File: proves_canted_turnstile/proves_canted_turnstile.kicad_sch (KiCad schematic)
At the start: 11 parts, among them J1 Conn_Coaxial, U1 QBA-07+, U2 QBA-07+, U3 QBA-07+

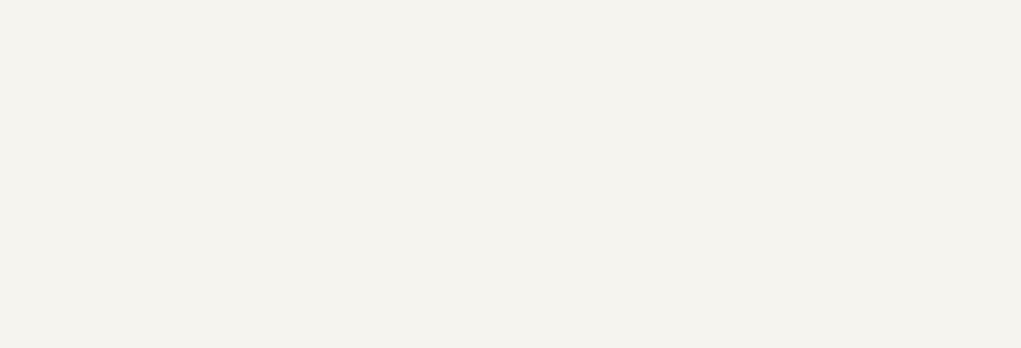
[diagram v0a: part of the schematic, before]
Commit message: assigned footprints to symbols and imported fiducials
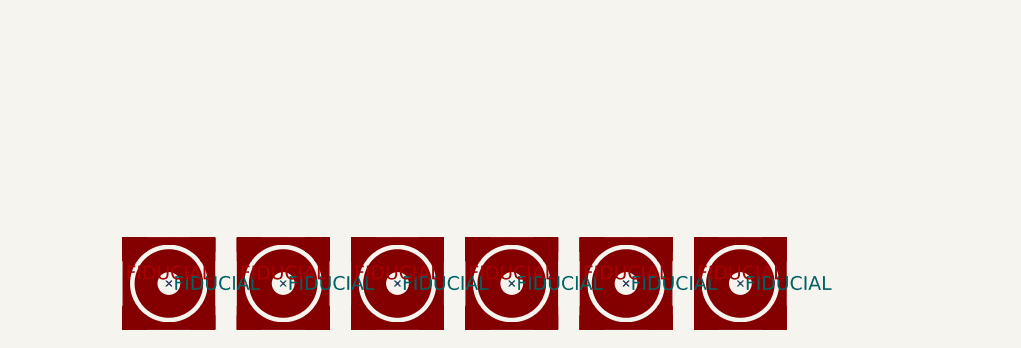
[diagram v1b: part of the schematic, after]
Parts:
- added FIDUCIAL1, FIDUCIAL2, FIDUCIAL3, FIDUCIAL4, FIDUCIAL6, FIDUCIAL7: FIDUCIAL-1.0X2.0, plusz-end-card-with-turnstile-mezzanine-eagle-import:FIDUCIAL-1.0X2.0, symbol plusz-end-card-with-turnstile-mezzanine-eagle-import:FIDUCIAL-1.0X2.0
- R1, R2, R3: footprint plusz-end-card-with-turnstile-mezzanine:.0603-C-NOSILK -> plusz-end-card-with-turnstile-mezzanine-eagle-import:.0603-C-NOSILK
- U1, U2, U3: footprint plusz-end-card-with-turnstile-mezzanine:QBA-07+ -> plusz-end-card-with-turnstile-mezzanine-eagle-import:QBA-07+

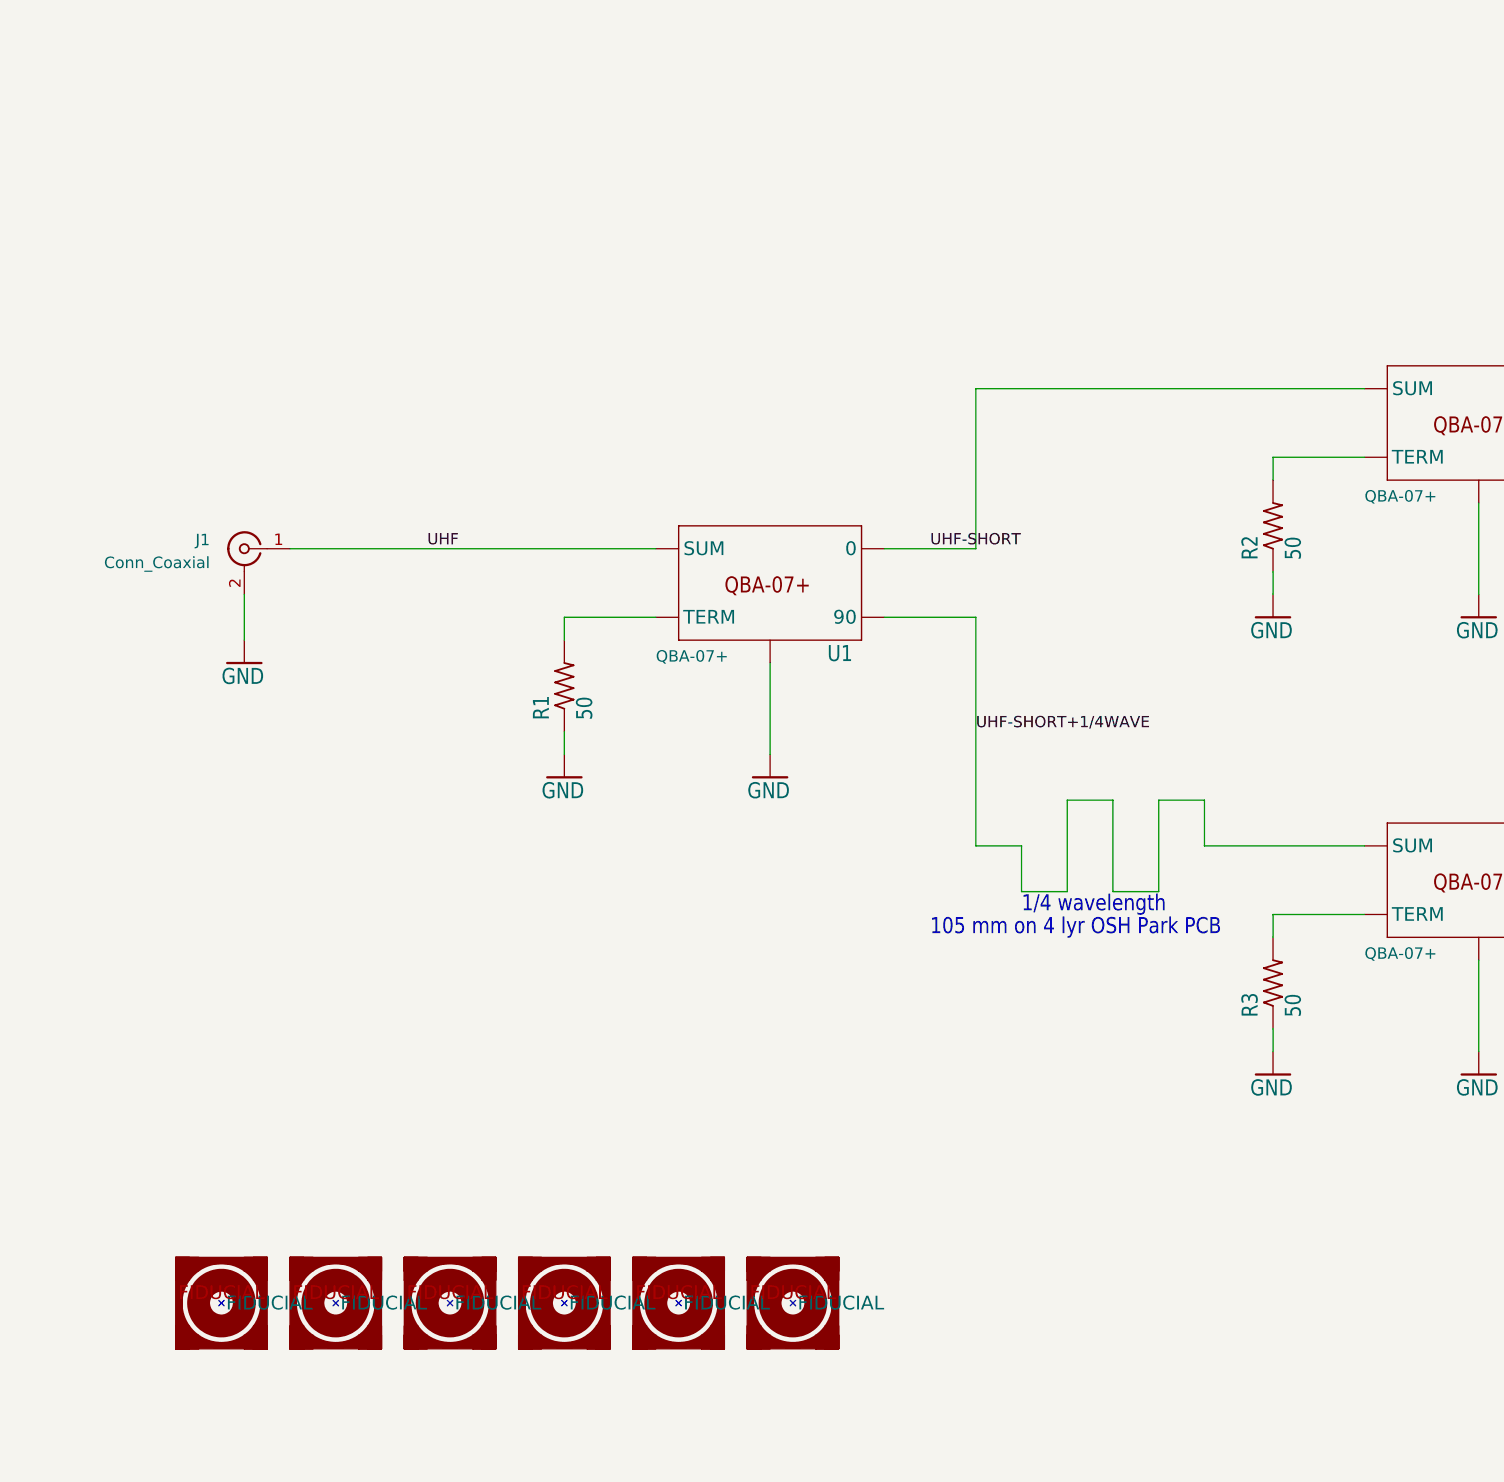
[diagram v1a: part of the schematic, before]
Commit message: implemented burnwire in schematic
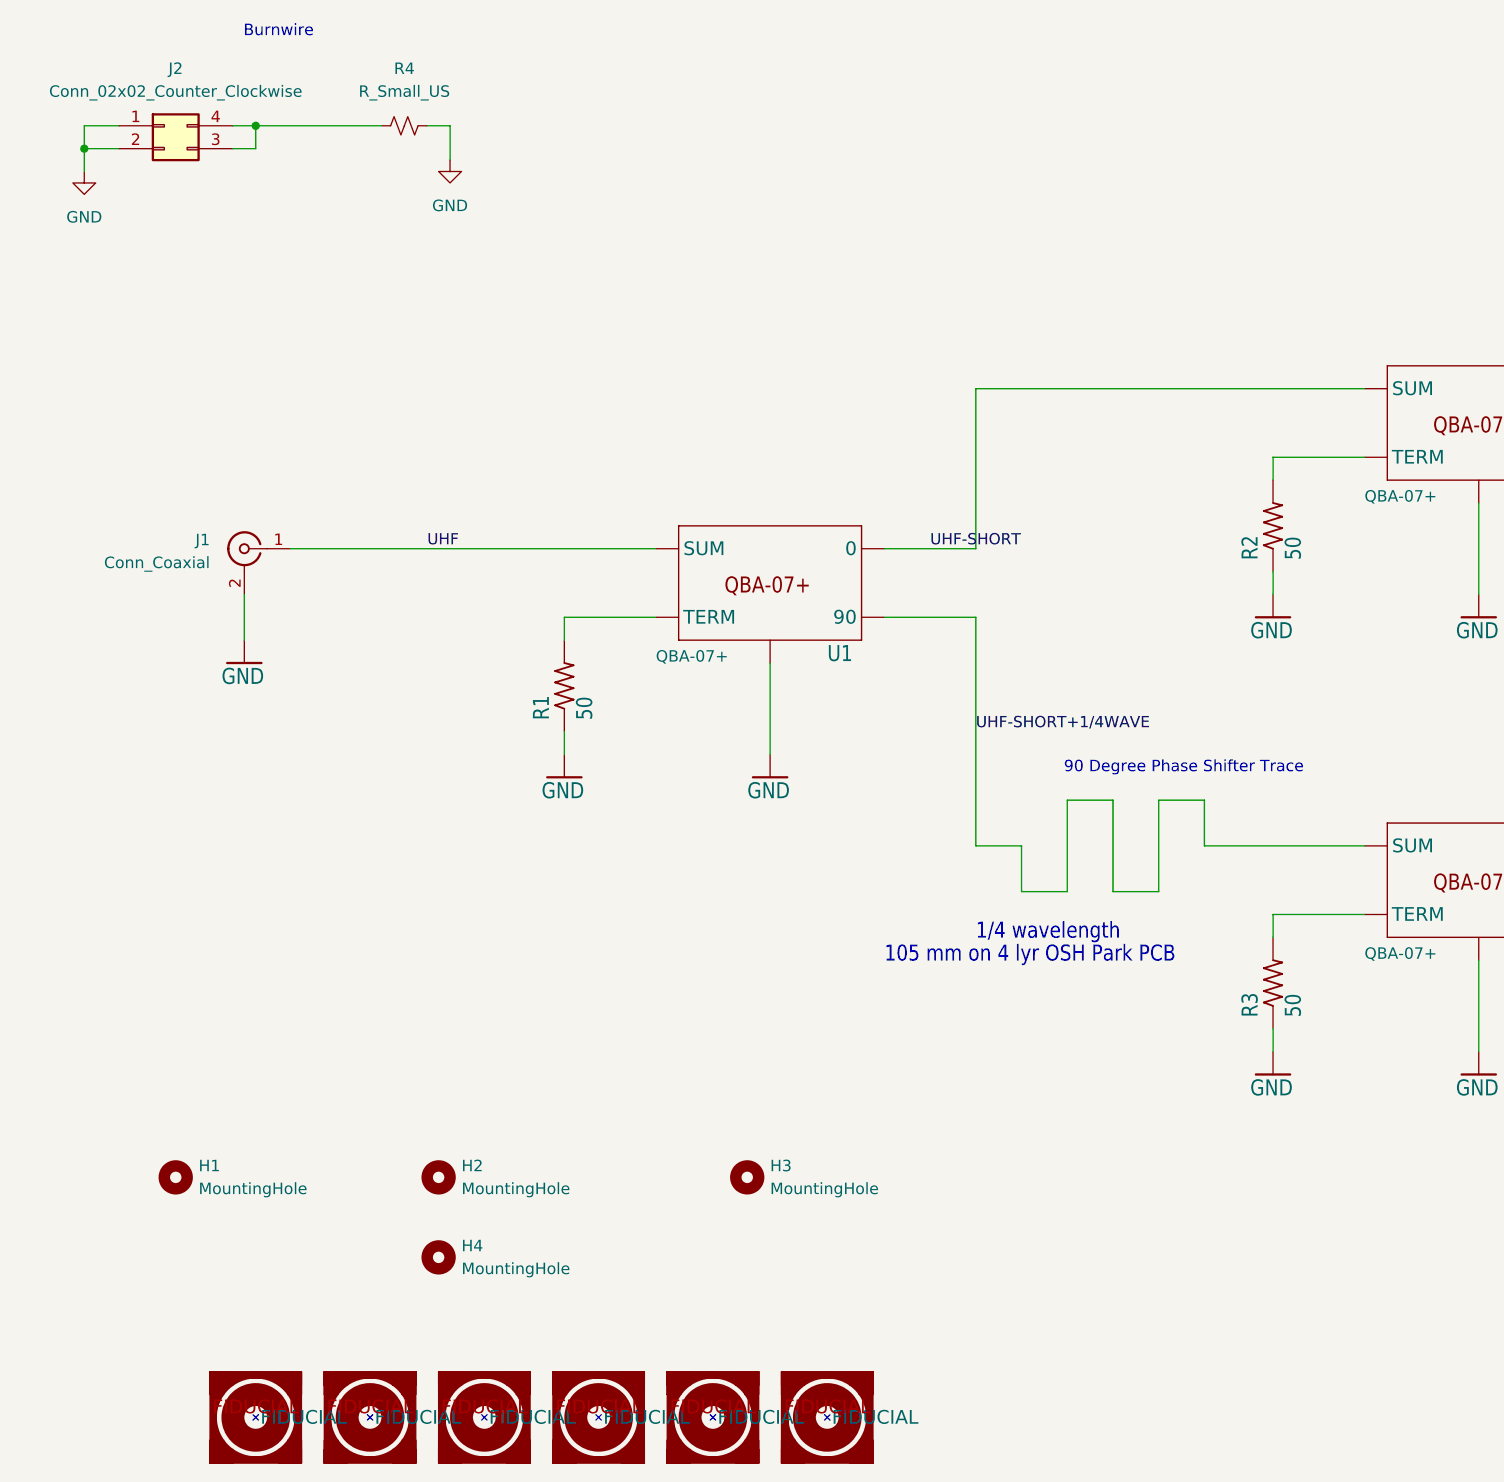
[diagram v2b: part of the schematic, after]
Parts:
- added H1, H2, H3, H4: MountingHole, MountingHole:MountingHole_2.7mm_M2.5_Pad, symbol Mechanical:MountingHole
- added J2: Conn_02x02_Counter_Clockwise, symbol Connector_Generic:Conn_02x02_Counter_Clockwise
- added R4: R_Small_US, symbol Device:R_Small_US
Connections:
- net GND: now also J2.1 (Pin_1), J2.2 (Pin_2), R4.2
- new net: J2.3 (Pin_3), J2.4 (Pin_4), R4.1
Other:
- note added: "90 Degree Phase Shifter Trace"
- note added: "Burnwire"

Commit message: updates
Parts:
- J2: footprint (none) -> Connector_Hirose:Hirose_DF11-4DP-2DSA_2x02_P2.00mm_Vertical
- R4: footprint (none) -> Resistor_THT:R_Axial_DIN0411_L9.9mm_D3.6mm_P25.40mm_Horizontal
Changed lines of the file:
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@@
 			)
 		)
-		(property "Footprint" ""
+		(property "Footprint" "Resistor_THT:R_Axial_DIN0411_L9.9mm_D3.6mm_P25.40mm_Horizontal"
 			(at 64.77 29.21 0)
 			(effects
@@
 			)
 		)
-		(property "Footprint" ""
+		(property "Footprint" "Connector_Hirose:Hirose_DF11-4DP-2DSA_2x02_P2.00mm_Vertical"
 			(at 38.1 29.21 0)
 			(effects

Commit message: changed trace widths
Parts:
- AE1, AE2, AE3, AE4: footprint Turnstile_Library:Singular_Tape_Measure_Antenna -> plusz-end-card-with-turnstile-mezzanine-eagle-import:Singular Tape Measure
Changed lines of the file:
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@@
 			)
 		)
-		(property "Footprint" "Turnstile_Library:Singular_Tape_Measure_Antenna"
+		(property "Footprint" "plusz-end-card-with-turnstile-mezzanine-eagle-import:Singular Tape Measure"
 			(at 237.49 66.04 0)
 			(effects
@@
 			)
 		)
-		(property "Footprint" "Turnstile_Library:Singular_Tape_Measure_Antenna"
+		(property "Footprint" "plusz-end-card-with-turnstile-mezzanine-eagle-import:Singular Tape Measure"
 			(at 237.49 111.76 0)
 			(effects
@@
 			)
 		)
-		(property "Footprint" "Turnstile_Library:Singular_Tape_Measure_Antenna"
+		(property "Footprint" "plusz-end-card-with-turnstile-mezzanine-eagle-import:Singular Tape Measure"
 			(at 237.49 43.18 0)
 			(effects
@@
 			)
 		)
-		(property "Footprint" "Turnstile_Library:Singular_Tape_Measure_Antenna"
+		(property "Footprint" "plusz-end-card-with-turnstile-mezzanine-eagle-import:Singular Tape Measure"
 			(at 237.49 88.9 0)
 			(effects

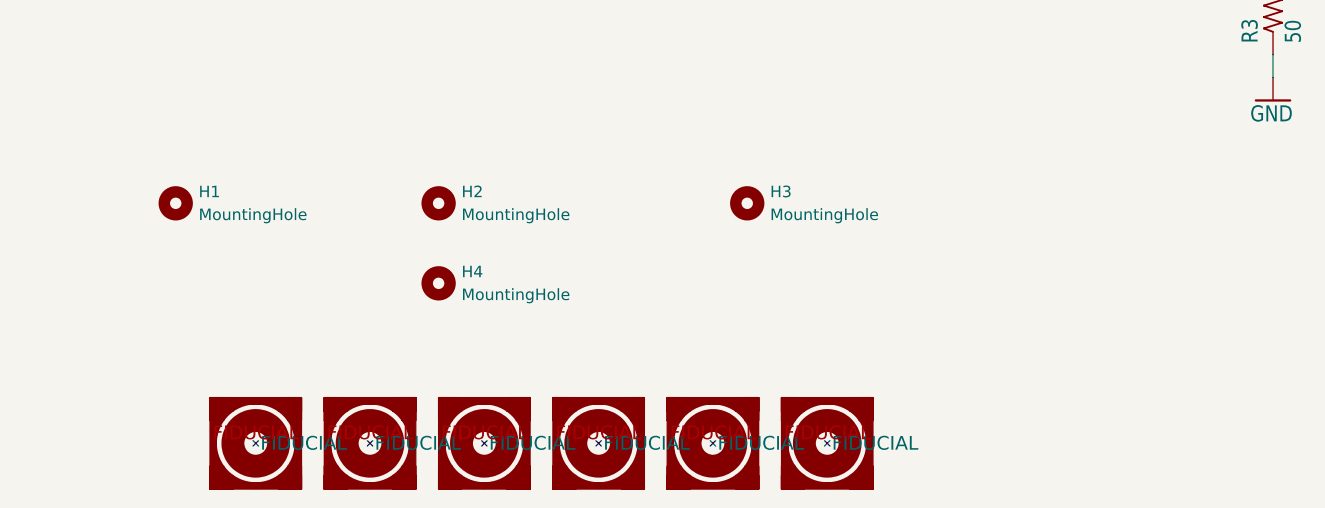
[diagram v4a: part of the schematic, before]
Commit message: placed mounting holes
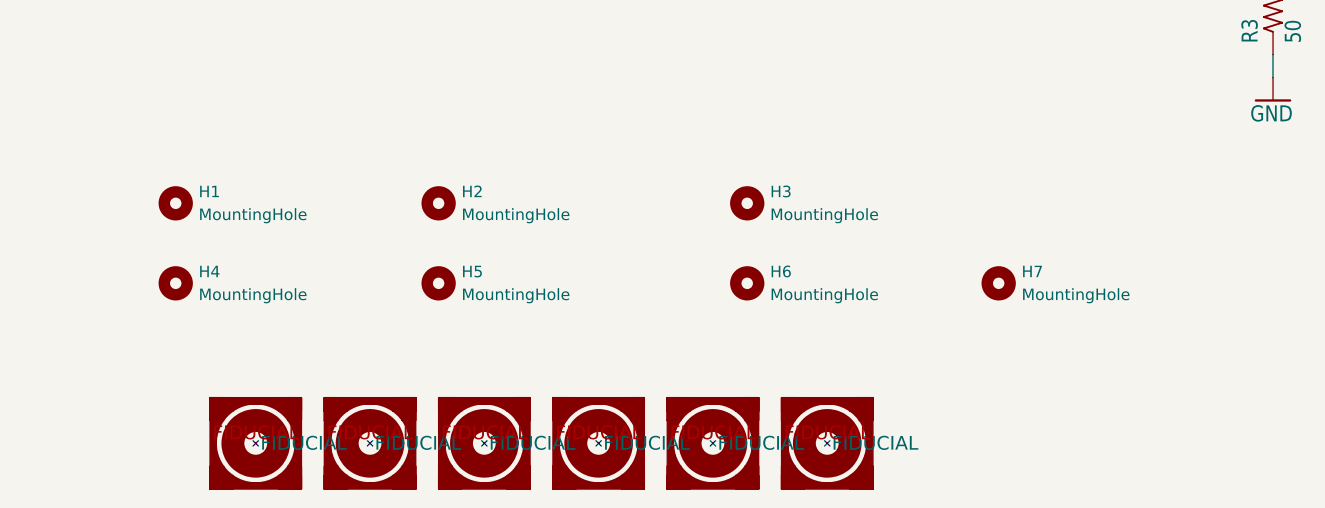
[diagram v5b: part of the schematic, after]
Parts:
- added H5, H6, H7: MountingHole, MountingHole:MountingHole_2.7mm_M2.5_Pad, symbol Mechanical:MountingHole
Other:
- moved on the sheet: H4
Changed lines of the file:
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@@
+	)
+	(symbol
+		(lib_id "Mechanical:MountingHole")
+		(at 102.87 154.94 0)
+		(unit 1)
+		(exclude_from_sim yes)
+		(in_bom no)
+		(on_board yes)
+		(dnp no)
+		(fields_autoplaced yes)
+		(property "Reference" "H6"
+			(at 105.41 153.6699 0)
+			(effects
+				(font
+					(size 1.27 1.27)
+				)
+				(justify left)
+			)
+		)
+		(property "Value" "MountingHole"
+			(at 105.41 156.2099 0)
+			(effects
+				(font
+					(size 1.27 1.27)
+				)
+				(justify left)
+			)
+		)
+		(property "Footprint" "MountingHole:MountingHole_2.7mm_M2.5_Pad"
+			(at 102.87 154.94 0)
+			(effects
+				(font
+					(size 1.27 1.27)
+				)
+				(hide yes)
+			)
+		)
+		(property "Datasheet" "~"
+			(at 102.87 154.94 0)
+			(effects
+				(font
+					(size 1.27 1.27)
+				)
+				(hide yes)
+			)
+		)
+		(property "Description" "Mounting Hole without connection"
+			(at 102.87 154.94 0)
+			(effects
+				(font
+					(size 1.27 1.27)
+				)
+				(hide yes)
+			)
+		)
+		(instances
+			(project "proves_canted_turnstile"
+				(path "/b0a1b345-df47-405c-b751-07790b55dab3"
+					(reference "H6")
+					(unit 1)
+				)
+			)
+		)
 	)
 	(symbol
@@
 	(symbol
 		(lib_id "Mechanical:MountingHole")
-		(at 68.58 154.94 0)
+		(at 39.37 154.94 0)
 		(unit 1)
 		(exclude_from_sim yes)
@@
 		(fields_autoplaced yes)
 		(property "Reference" "H4"
-			(at 71.12 153.6699 0)
+			(at 41.91 153.6699 0)
 			(effects
 				(font
@@
 		)
 		(property "Value" "MountingHole"
-			(at 71.12 156.2099 0)
+			(at 41.91 156.2099 0)
 			(effects
 				(font
@@
 		)
 		(property "Footprint" "MountingHole:MountingHole_2.7mm_M2.5_Pad"
-			(at 68.58 154.94 0)
+			(at 39.37 154.94 0)
 			(effects
 				(font
@@
 		)
 		(property "Datasheet" "~"
-			(at 68.58 154.94 0)
+			(at 39.37 154.94 0)
 			(effects
 				(font
@@
 		)
 		(property "Description" "Mounting Hole without connection"
-			(at 68.58 154.94 0)
+			(at 39.37 154.94 0)
 			(effects
 				(font
@@
 					(unit 1)
 				)
+			)
+		)
+	)
+	(symbol
+		(lib_id "Mechanical:MountingHole")
+		(at 68.58 154.94 0)
+		(unit 1)
+		(exclude_from_sim yes)
+		(in_bom no)
+		(on_board yes)
+		(dnp no)
+		(fields_autoplaced yes)
+		(property "Reference" "H5"
+			(at 71.12 153.6699 0)
+			(effects
+				(font
+					(size 1.27 1.27)
+				)
+				(justify left)
+			)
+		)
+		(property "Value" "MountingHole"
+			(at 71.12 156.2099 0)
+			(effects
+				(font
+					(size 1.27 1.27)
+				)
+				(justify left)
+			)
+		)
+		(property "Footprint" "MountingHole:MountingHole_2.7mm_M2.5_Pad"
+			(at 68.58 154.94 0)
+			(effects
+				(font
+					(size 1.27 1.27)
+				)
+				(hide yes)
+			)
+		)
+		(property "Datasheet" "~"
+			(at 68.58 154.94 0)
+			(effects
+				(font
+					(size 1.27 1.27)
+				)
+				(hide yes)
+			)
+		)
+		(property "Description" "Mounting Hole without connection"
+			(at 68.58 154.94 0)
+			(effects
+				(font
+					(size 1.27 1.27)
+				)
+				(hide yes)
+			)
+		)
+		(instances
+			(project "proves_canted_turnstile"
+				(path "/b0a1b345-df47-405c-b751-07790b55dab3"
+					(reference "H5")
+					(unit 1)
+				)
+			)
+		)
+	)
+	(symbol
+		(lib_id "Mechanical:MountingHole")
+		(at 130.81 154.94 0)
+		(unit 1)
+		(exclude_from_sim yes)
+		(in_bom no)
+		(on_board yes)
+		(dnp no)
+		(fields_autoplaced yes)
+		(property "Reference" "H7"
+			(at 133.35 153.6699 0)
+			(effects
+				(font
+					(size 1.27 1.27)
+				)
+				(justify left)
+			)
+		)
+		(property "Value" "MountingHole"
+			(at 133.35 156.2099 0)
+			(effects
+				(font
+					(size 1.27 1.27)
+				)
+				(justify left)
+			)
+		)
+		(property "Footprint" "MountingHole:MountingHole_2.7mm_M2.5_Pad"
+			(at 130.81 154.94 0)
+			(effects
+				(font
+					(size 1.27 1.27)
+				)
+				(hide yes)
+			)
+		)
+		(property "Datasheet" "~"
+			(at 130.81 154.94 0)
+			(effects
+				(font
+					(size 1.27 1.27)
+				)
+				(hide yes)
+			)
+		)
+		(property "Description" "Mounting Hole without connection"
+			(at 130.81 154.94 0)
+			(effects
+				(font
+					(size 1.27 1.27)
+				)
+				(hide yes)
+			)
+		)
+		(instances
+			(project "proves_canted_turnstile"
+				(path "/b0a1b345-df47-405c-b751-07790b55dab3"
+					(reference "H7")
+					(unit 1)
+				)
